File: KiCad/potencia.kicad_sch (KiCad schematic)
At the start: 16 parts, among them K1 Fujitsu_FTR-LYAA005x, K2 Fujitsu_FTR-LYAA005x, Q1 2N7002, Q2 2N7002

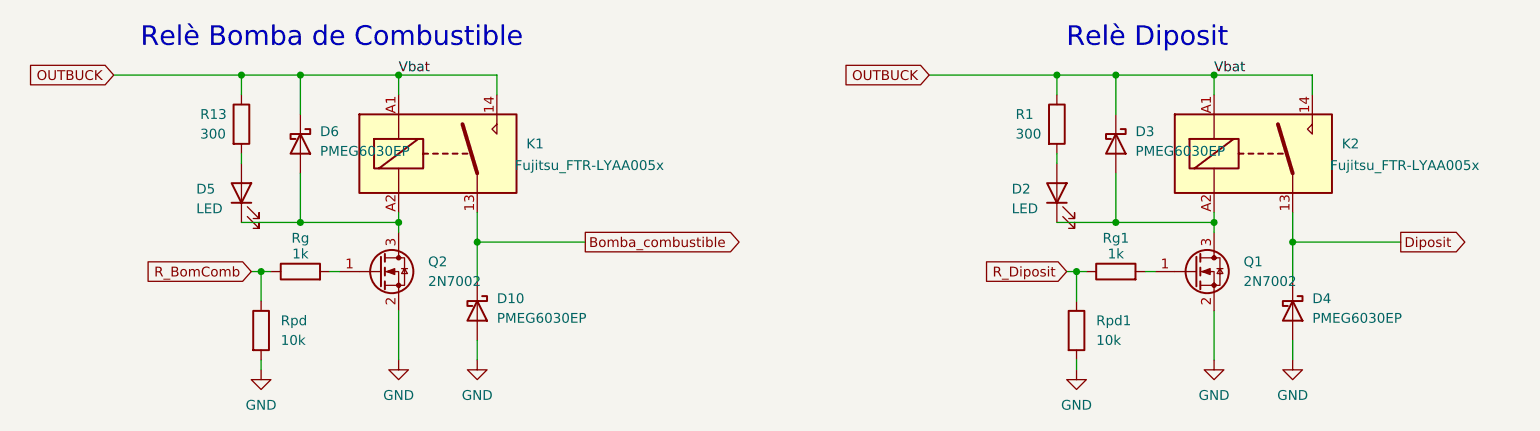
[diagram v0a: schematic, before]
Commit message: Arreglat els pins i cambiat el model del relé
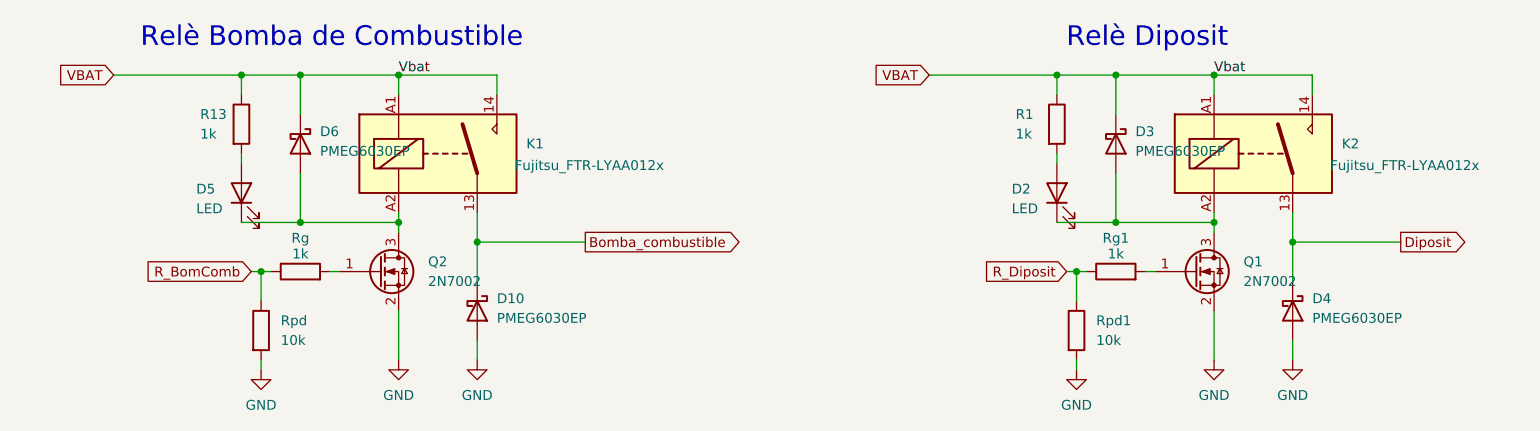
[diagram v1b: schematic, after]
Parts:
- K1, K2: value Fujitsu_FTR-LYAA005x -> Fujitsu_FTR-LYAA012x
- R1, R13: value 300 -> 1k
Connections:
- net OUTBUCK renamed VBAT
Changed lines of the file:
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@@
 		)
 	)
-	(global_label "OUTBUCK"
+	(global_label "VBAT"
 		(shape input)
 		(at 50.8 54.61 180)
@@
 		)
 		(property "Intersheetrefs" "${INTERSHEET_REFS}"
-			(at 39.0457 54.61 0)
+			(at 43.4 54.61 0)
 			(effects
 				(font
@@
 		)
 	)
-	(global_label "OUTBUCK"
+	(global_label "VBAT"
 		(shape input)
 		(at 156.21 54.61 180)
@@
 		)
 		(property "Intersheetrefs" "${INTERSHEET_REFS}"
-			(at 144.4557 54.61 0)
+			(at 148.81 54.61 0)
 			(effects
 				(font
@@
 			)
 		)
-		(property "Value" "300"
+		(property "Value" "1k"
 			(at 61.976 62.23 0)
 			(effects
@@
 			)
 		)
-		(property "Value" "300"
+		(property "Value" "1k"
 			(at 167.386 62.23 0)
 			(effects
@@
 			)
 		)
-		(property "Value" "Fujitsu_FTR-LYAA005x"
+		(property "Value" "Fujitsu_FTR-LYAA012x"
 			(at 208.026 66.294 0)
 			(effects
@@
 			)
 		)
-		(property "Value" "Fujitsu_FTR-LYAA005x"
+		(property "Value" "Fujitsu_FTR-LYAA012x"
 			(at 102.616 66.294 0)
 			(effects

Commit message: Part de potencia moguda al sheet de analogica, esborrat el sheet de potencia
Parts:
- removed D10, D3, D4, D6: PMEG6030EP, Diode_SMD:D_SOD-128, symbol Diode:PMEG6030EP
- removed D2, D5: LED, LED_SMD:LED_0805_2012Metric, symbol Device:LED
- removed K1, K2: Fujitsu_FTR-LYAA012x, Relay_THT:Relay_SPST-NO_Fujitsu_FTR-LYAA005x_FormA_Vertical, symbol Relay:Fujitsu_FTR-LYAA005x
- removed Q1, Q2: 2N7002, Package_TO_SOT_SMD:SOT-23, symbol Transistor_FET:2N7002
- removed R1, R13, Rg, Rg1: 1k, Resistor_SMD:R_1206_3216Metric, symbol Device:R
- removed Rpd, Rpd1: 10k, Resistor_SMD:R_1206_3216Metric, symbol Device:R
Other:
- note removed: "Relè Bomba de Combustible"
- note removed: "Relè Diposit"
